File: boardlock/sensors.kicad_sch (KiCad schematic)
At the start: 16 parts, among them Q1 Q_PMOS_GSD, Q2 Q_NPN_BCE, Q3 Q_NPN_BCE, Q4 Q_PMOS_GSD, U1 LSM6DS3, U2 SAM-M8Q

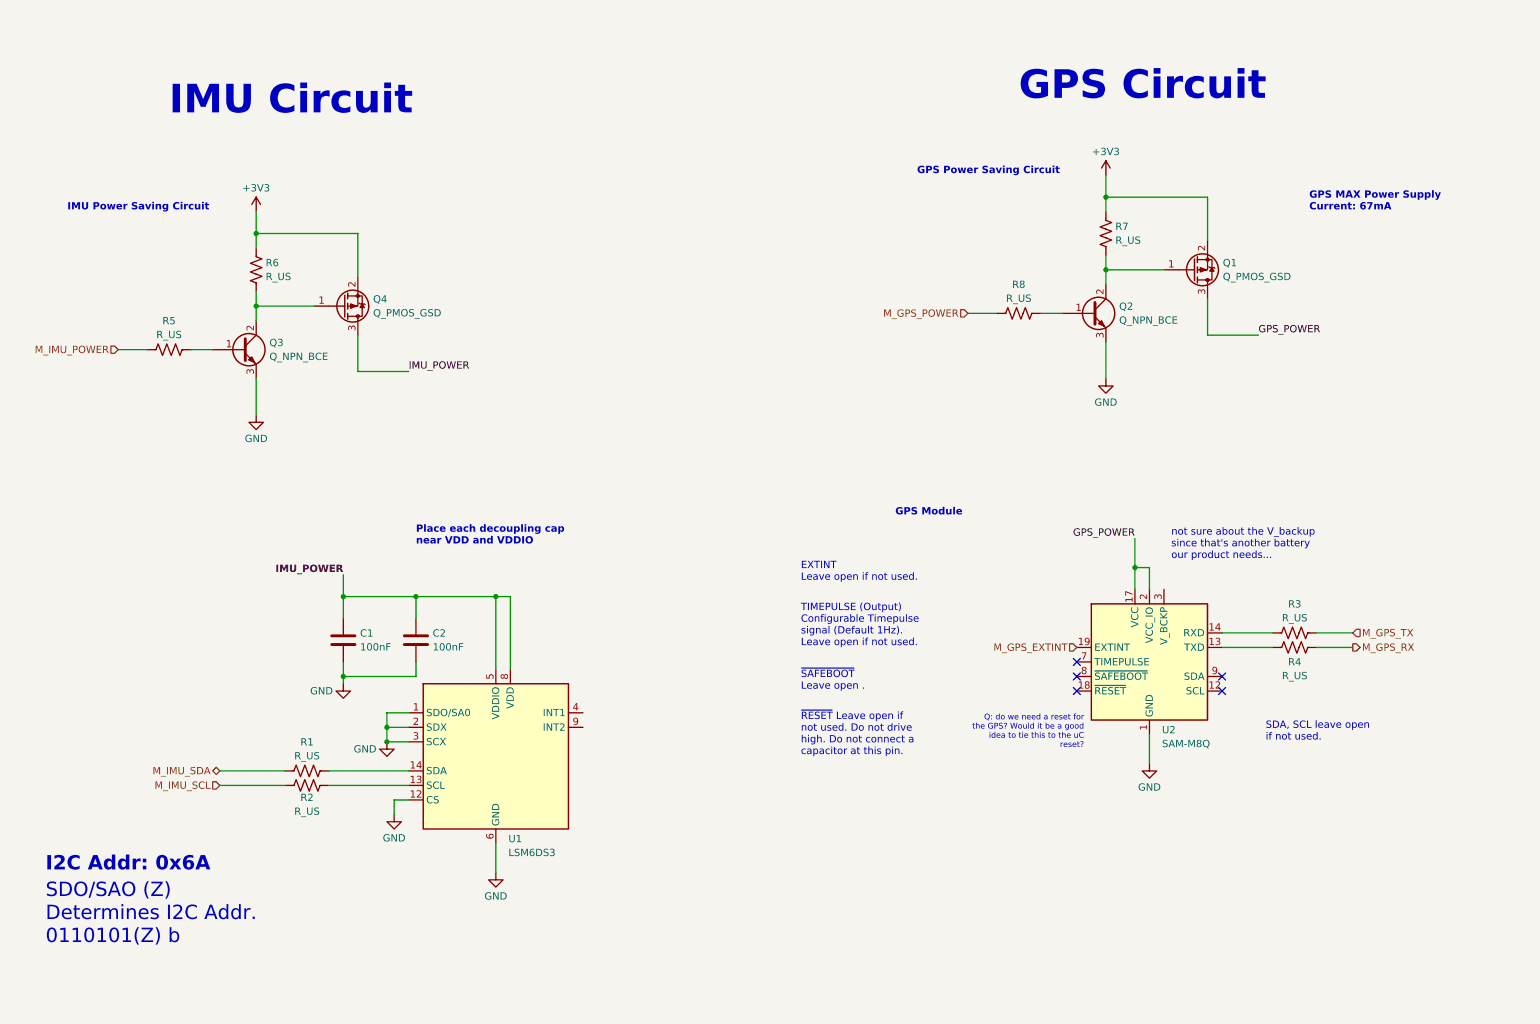
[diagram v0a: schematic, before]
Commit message: GPS I2C version
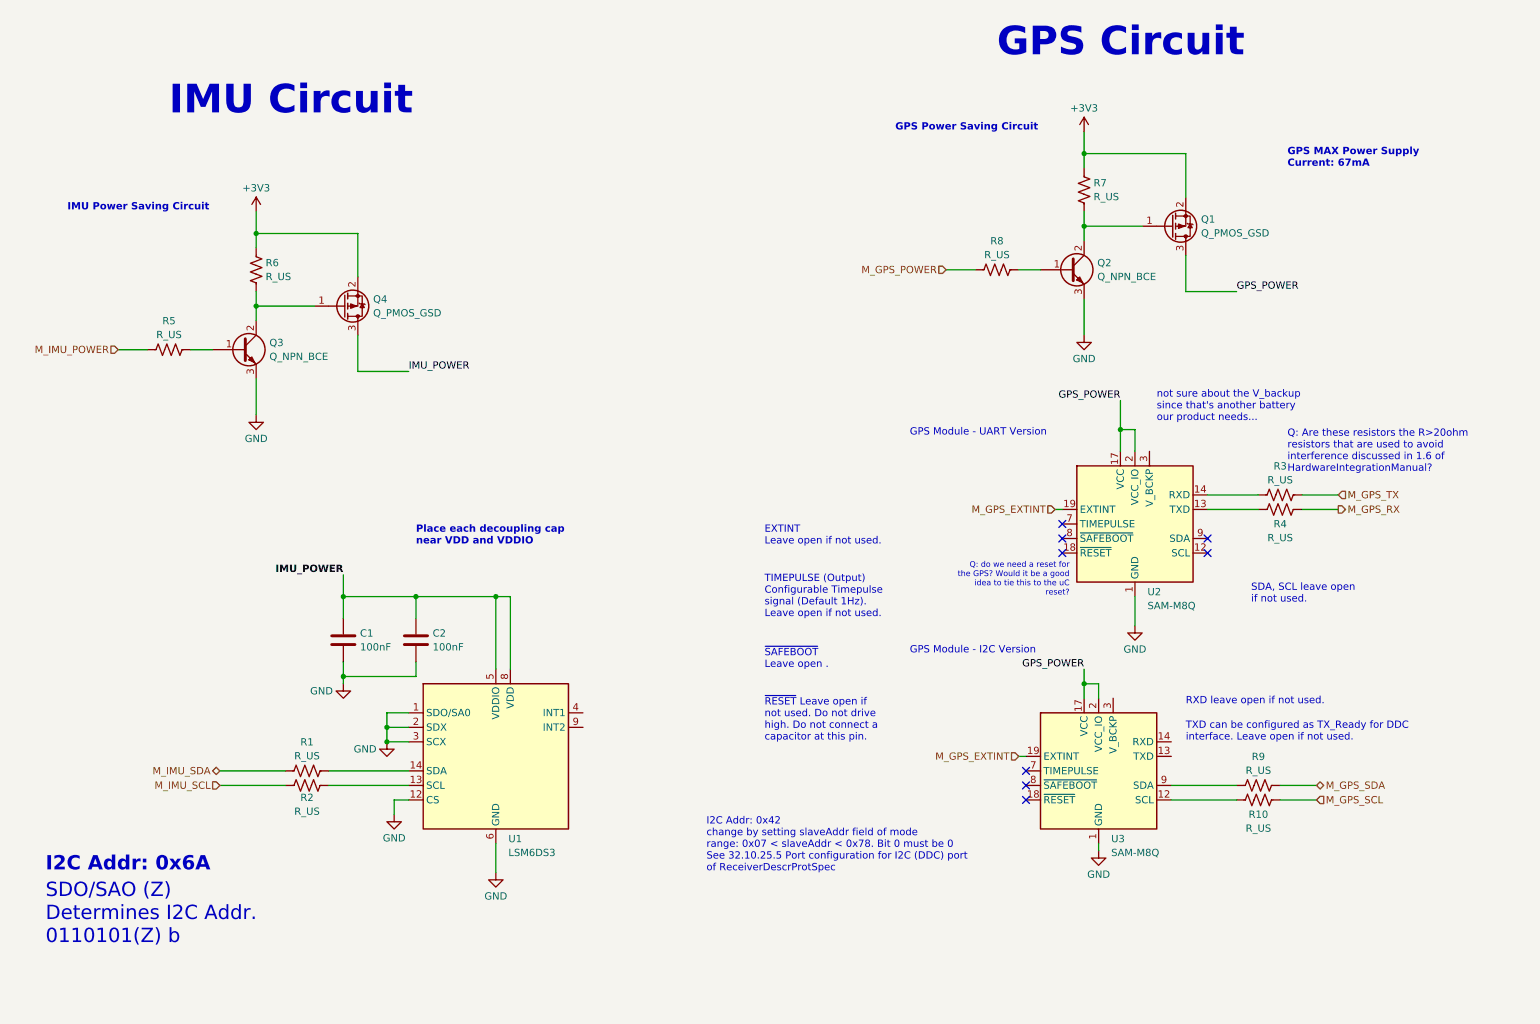
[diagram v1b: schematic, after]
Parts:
- added R10, R9: R_US, symbol Device:R_US
- added U3: SAM-M8Q, RF_GPS:ublox_SAM-M8Q, symbol RF_GPS:SAM-M8Q
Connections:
- net GND: now also U3.1 (GND), U3.10 (GND), U3.11 (GND), U3.15 (GND), U3.16 (GND), U3.20 (GND), U3.4 (GND), U3.5 (GND), U3.6 (GND)
- net GPS_POWER: now also U3.17 (VCC), U3.2 (VCC_IO)
- net M_GPS_EXTINT: now also U3.19 (EXTINT)
- new net: R9.2, U3.9 (SDA)
- new net: R10.2, U3.12 (SCL)
- new net M_GPS_SCL: R10.1
- new net M_GPS_SDA: R9.1
- no-connect marks 5 -> 8
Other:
- note added: "GPS Module - I2C Version"
- note added: "GPS Module - UART Version"
- note added: "I2C Addr: 0x42 change by setting slaveAddr field of mode range: 0x07 < slaveAddr < 0x78. Bit 0 must be 0 See 32.10.25.5 Port configuration for I2C (DDC) port of ReceiverDescrProtSpec"
- note added: "Q: Are these resistors the R>20ohm resistors that are used to avoid interference discussed in 1.6 of HardwareIntegrationManual?"
- note added: "RXD leave open if not used."
- note added: "TXD can be configured as TX_Ready for DDC interface. Leave open if not used."
- note removed: "GPS Module"

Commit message: Added ESP32 library and SCH edits
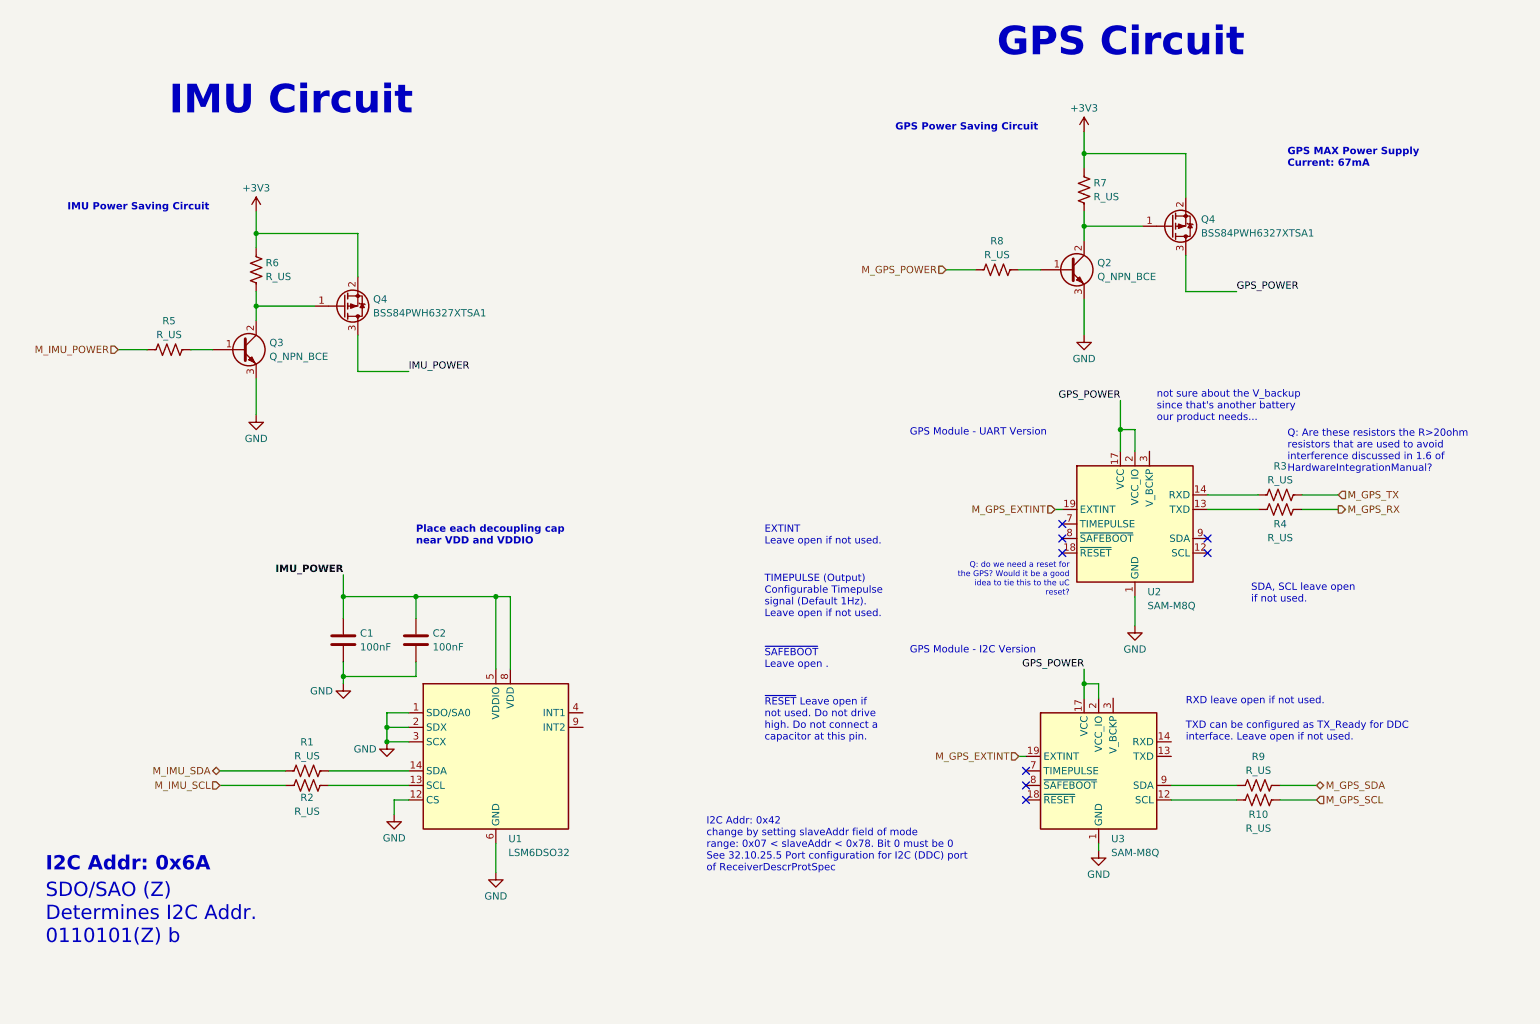
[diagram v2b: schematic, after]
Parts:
- removed Q1: Q_PMOS_GSD, symbol Device:Q_PMOS_GSD
- added Q4: BSS84PWH6327XTSA1, Package_TO_SOT_SMD:SOT-323_SC-70_Handsoldering, symbol Device:Q_PMOS_GSD
- Q4: value Q_PMOS_GSD -> BSS84PWH6327XTSA1; footprint (none) -> Package_TO_SOT_SMD:SOT-323_SC-70_Handsoldering
- U1: value LSM6DS3 -> LSM6DSO32
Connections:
- net +3V3: now also Q4.2 (S)
- net GPS_POWER: now also Q4.3 (D)
- net at Q2.2 (C), R7.2: now also Q4.1 (G)
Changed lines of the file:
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@@
-    )
-  )
-  (symbol (lib_id "Device:Q_PMOS_GSD") (at 227.33 50.8 0) (mirror x) (unit 1)
-    (in_bom yes) (on_board yes) (dnp no) (fields_autoplaced)
-    (property "Reference" "Q1" (at 232.537 49.5879 0)
-      (effects (font (size 1.27 1.27)) (justify left))
-    )
-    (property "Value" "Q_PMOS_GSD" (at 232.537 52.0121 0)
-      (effects (font (size 1.27 1.27)) (justify left))
-    )
-    (property "Footprint" "" (at 232.41 53.34 0)
-      (effects (font (size 1.27 1.27)) hide)
-    )
-    (property "Datasheet" "~" (at 227.33 50.8 0)
-      (effects (font (size 1.27 1.27)) hide)
-    )
-    (pin "1")
-    (pin "2")
-    (pin "3")
-    (instances
-      (project "boardlock"
-        (path "/48f24f42-fd64-4860-9f12-ca34cf195758/17b4aebf-aea4-4bb2-a07c-86de8cf47820"
-          (reference "Q1") (unit 1)
-        )
-      )
-      (project "boardlock"
-        (path "/e1fc29ce-837e-4062-84d8-c7e423f9eab9/a4a6f965-a4d9-4da6-b64e-79eda0daabe5"
-          (reference "Q3") (unit 1)
-        )
-      )
     )
   )
@@
       (effects (font (size 1.27 1.27)) (justify left))
     )
-    (property "Value" "LSM6DS3" (at 111.4141 160.3543 0)
+    (property "Value" "LSM6DSO32" (at 111.4141 160.3543 0)
       (effects (font (size 1.27 1.27)) (justify left))
     )
@@
       (effects (font (size 1.27 1.27)) (justify left) hide)
     )
-    (property "Datasheet" "https://www.st.com/resource/en/datasheet/lsm6ds3tr-c.pdf" (at 111.76 160.02 0)
+    (property "Datasheet" "https://www.st.com/resource/en/datasheet/lsm6dso32.pdf" (at 111.76 160.02 0)
       (effects (font (size 1.27 1.27)) hide)
     )
@@
         (path "/e1fc29ce-837e-4062-84d8-c7e423f9eab9/a4a6f965-a4d9-4da6-b64e-79eda0daabe5"
           (reference "#PWR07") (unit 1)
+        )
+      )
+    )
+  )
+  (symbol (lib_id "Device:Q_PMOS_GSD") (at 227.33 50.8 0) (mirror x) (unit 1)
+    (in_bom yes) (on_board yes) (dnp no) (fields_autoplaced)
+    (property "Reference" "Q4" (at 232.537 49.5879 0)
+      (effects (font (size 1.27 1.27)) (justify left))
+    )
+    (property "Value" "BSS84PWH6327XTSA1" (at 232.537 52.0121 0)
+      (effects (font (size 1.27 1.27)) (justify left))
+    )
+    (property "Footprint" "Package_TO_SOT_SMD:SOT-323_SC-70_Handsoldering" (at 232.41 53.34 0)
+      (effects (font (size 1.27 1.27)) hide)
+    )
+    (property "Datasheet" "https://www.infineon.com/dgdl/Infineon-BSS84PW-DS-v01_05-en.pdf?fileId=db3a3043321e49940132482056d32474" (at 227.33 50.8 0)
+      (effects (font (size 1.27 1.27)) hide)
+    )
+    (pin "1")
+    (pin "2")
+    (pin "3")
+    (instances
+      (project "boardlock"
+        (path "/48f24f42-fd64-4860-9f12-ca34cf195758/17b4aebf-aea4-4bb2-a07c-86de8cf47820"
+          (reference "Q4") (unit 1)
+        )
+        (path "/48f24f42-fd64-4860-9f12-ca34cf195758/17b4aebf-aea4-4bb2-a07c-86de8cf47820/50767468-7b8a-48f0-9e61-53ec0e447e69"
+          (reference "Q4") (unit 1)
+        )
+      )
+      (project "boardlock"
+        (path "/e1fc29ce-837e-4062-84d8-c7e423f9eab9/a4a6f965-a4d9-4da6-b64e-79eda0daabe5"
+          (reference "Q3") (unit 1)
         )
       )
@@
       (effects (font (size 1.27 1.27)) (justify left))
     )
-    (property "Value" "Q_PMOS_GSD" (at 87.757 65.9821 0)
-      (effects (font (size 1.27 1.27)) (justify left))
-    )
-    (property "Footprint" "" (at 87.63 67.31 0)
-      (effects (font (size 1.27 1.27)) hide)
-    )
-    (property "Datasheet" "~" (at 82.55 64.77 0)
-      (effects (font (size 1.27 1.27)) hide)
-    )
+    (property "Value" "BSS84PWH6327XTSA1" (at 87.757 65.9821 0)
+      (effects (font (size 1.27 1.27)) (justify left))
+    )
+    (property "Footprint" "Package_TO_SOT_SMD:SOT-323_SC-70_Handsoldering" (at 87.63 67.31 0)
+      (effects (font (size 1.27 1.27)) hide)
+    )
+    (property "Datasheet" "https://www.infineon.com/dgdl/Infineon-BSS84PW-DS-v01_05-en.pdf?fileId=db3a3043321e49940132482056d32474" (at 82.55 64.77 0)
+      (effects (font (size 1.27 1.27)) hide)
+    )

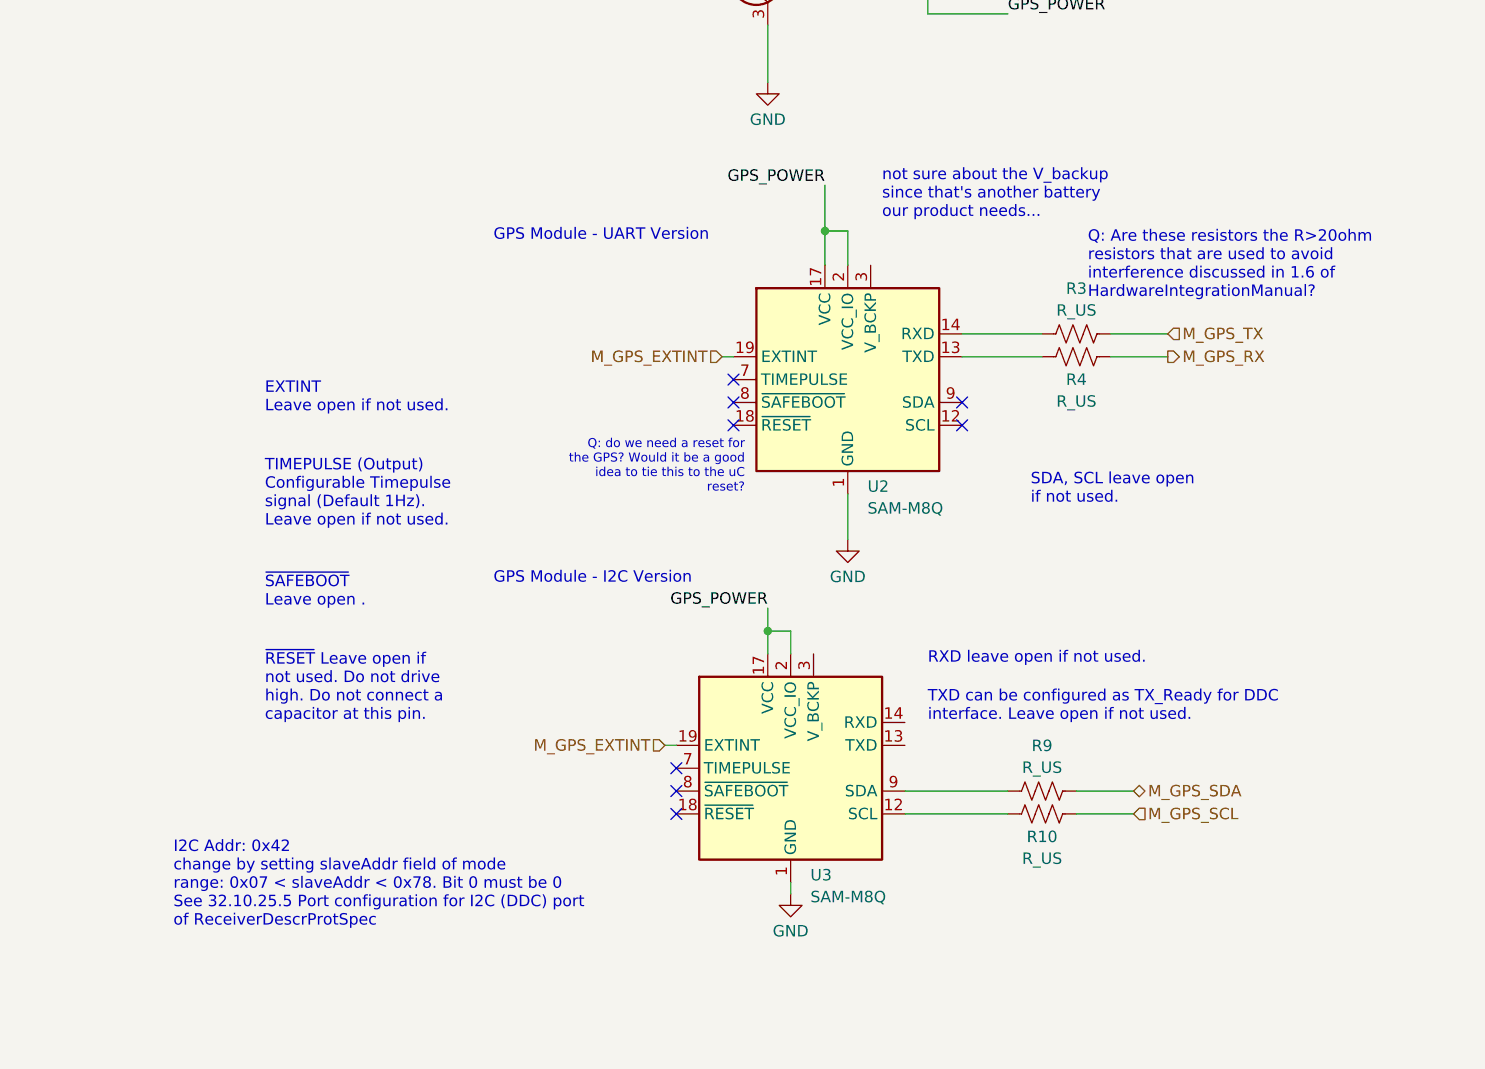
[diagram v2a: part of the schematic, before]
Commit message: deleted UART GPS
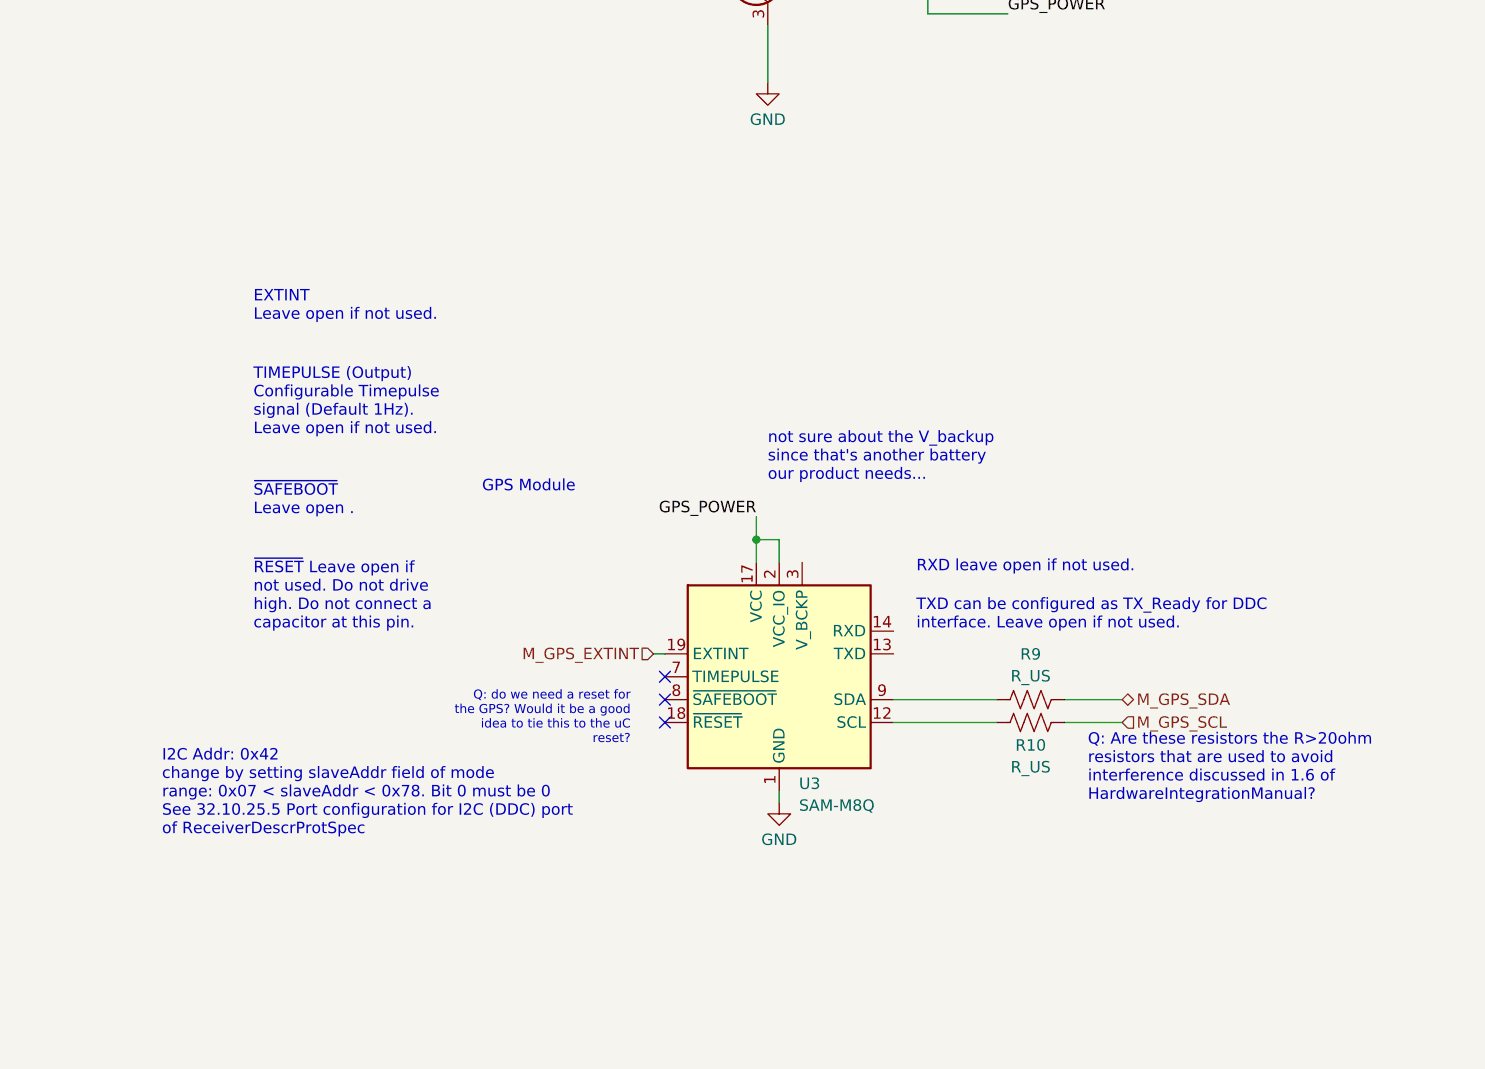
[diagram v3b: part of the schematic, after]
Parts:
- removed R3, R4: R_US, symbol Device:R_US
- removed U2: SAM-M8Q, RF_GPS:ublox_SAM-M8Q, symbol RF_GPS:SAM-M8Q
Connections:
- no-connect marks 8 -> 3
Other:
- note added: "GPS Module"
- note removed: "GPS Module - I2C Version"
- note removed: "GPS Module - UART Version"
- note removed: "SDA, SCL leave open if not used."
- moved on the sheet: R10, R9, U3
